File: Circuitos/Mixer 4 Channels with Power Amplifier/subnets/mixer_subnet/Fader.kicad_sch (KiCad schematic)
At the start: 4 parts, among them U5 ${SIM.PARAMS}

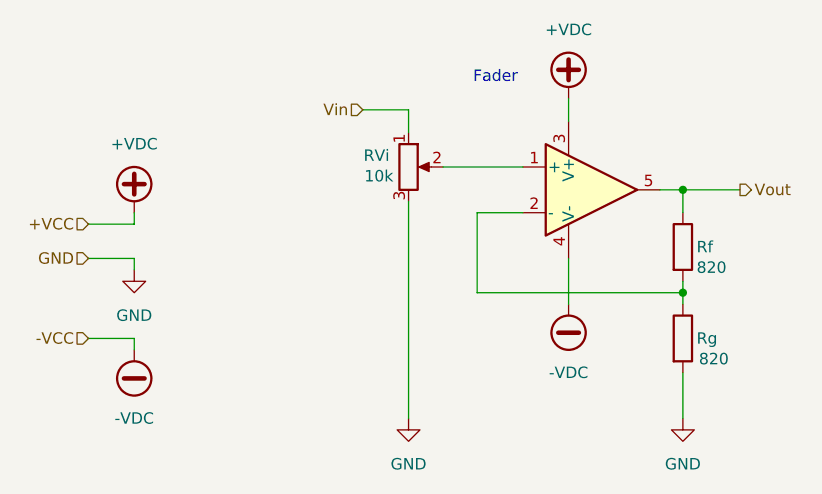
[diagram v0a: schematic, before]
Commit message: Correcciones y modificaciones en fuente, amp auriculares y simul completa
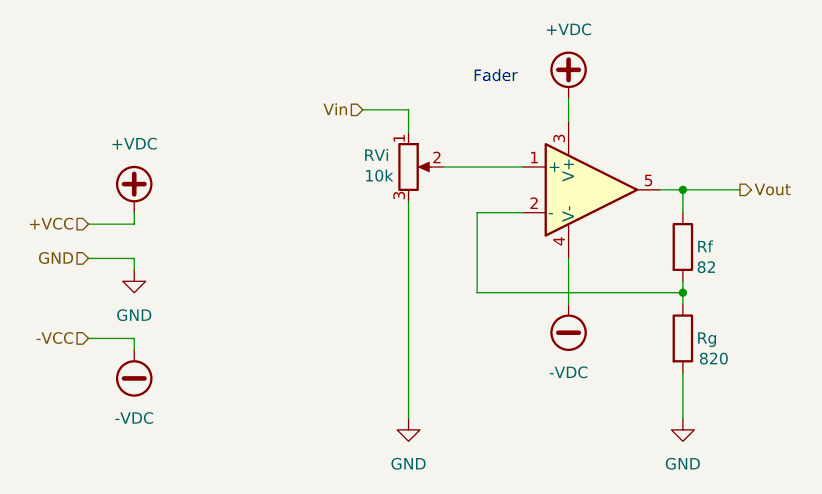
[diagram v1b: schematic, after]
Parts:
- Rf: value 820 -> 82
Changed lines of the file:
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@@
 			)
 		)
-		(property "Value" "820"
+		(property "Value" "82"
 			(at 146.304 84.836 0)
 			(effects
